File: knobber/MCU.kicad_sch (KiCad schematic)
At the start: 16 parts, among them J801 SWD, J802 Micro_SD_Card, U801 BMD-340-A-R, U802 ESD224DQA

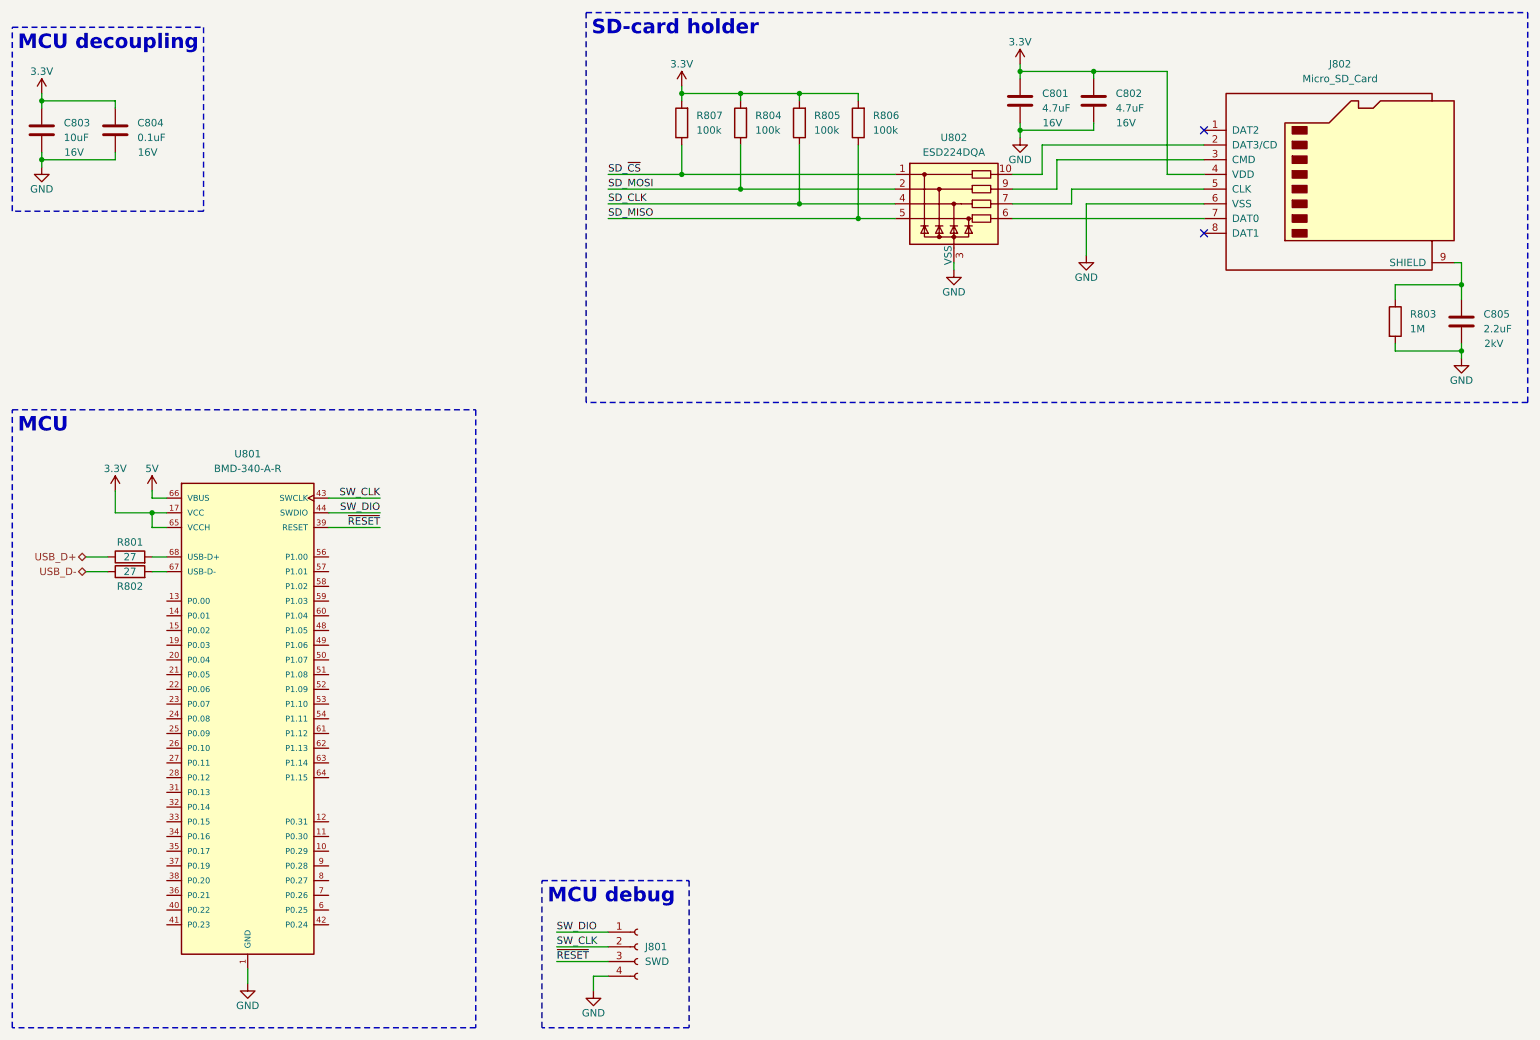
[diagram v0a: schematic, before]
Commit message: Updated schematic and PCB
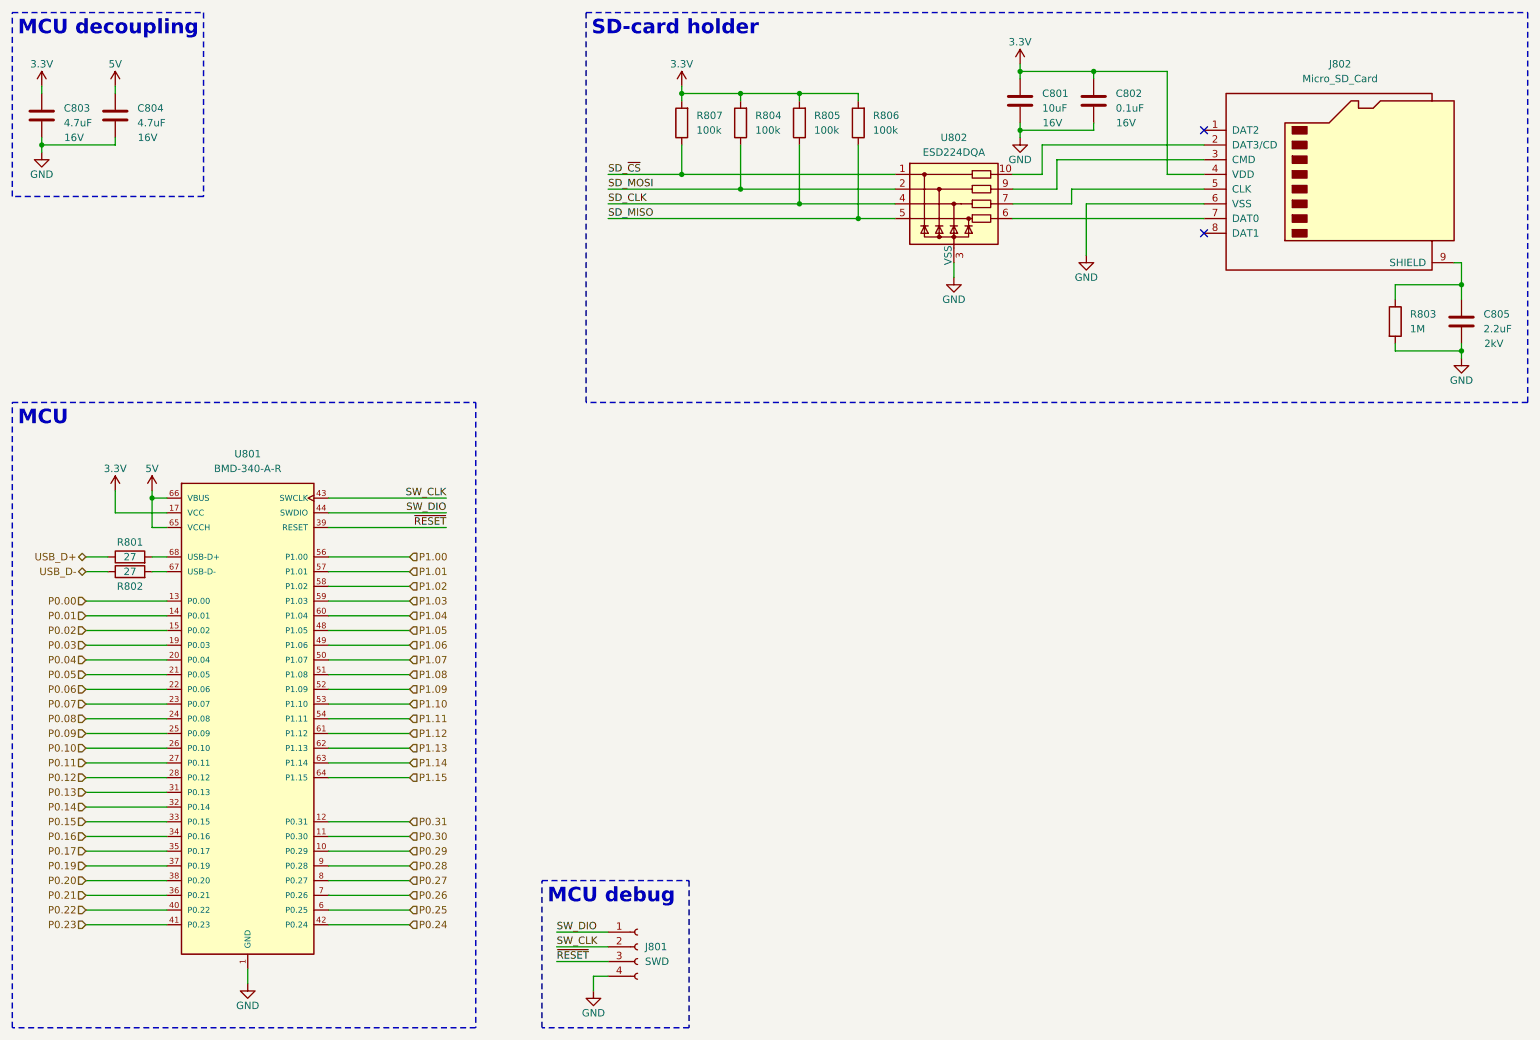
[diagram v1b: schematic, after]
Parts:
- C801: value 4.7uF -> 10uF
- C802: value 4.7uF -> 0.1uF
- C803: value 10uF -> 4.7uF
- C804: value 0.1uF -> 4.7uF
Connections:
- net 3.3V: no longer C804.1, U801.65 (VCCH)
- net 5V: now also C804.1, U801.65 (VCCH)
- net P0.29: now reaches U801.10 (P0.29)
- net P0.30: now reaches U801.11 (P0.30)
- net P0.31: now reaches U801.12 (P0.31)
- net P0.00: now reaches U801.13 (P0.00)
- net P0.01: now reaches U801.14 (P0.01)
- net P0.02: now reaches U801.15 (P0.02)
- net P0.03: now reaches U801.19 (P0.03)
- net P0.04: now reaches U801.20 (P0.04)
- net P0.05: now reaches U801.21 (P0.05)
- net P0.06: now reaches U801.22 (P0.06)
- net P0.07: now reaches U801.23 (P0.07)
- net P0.08: now reaches U801.24 (P0.08)
- net P0.09: now reaches U801.25 (P0.09)
- net P0.10: now reaches U801.26 (P0.10)
- net P0.11: now reaches U801.27 (P0.11)
- net P0.12: now reaches U801.28 (P0.12)
- net P0.13: now reaches U801.31 (P0.13)
- net P0.14: now reaches U801.32 (P0.14)
- net P0.15: now reaches U801.33 (P0.15)
- net P0.16: now reaches U801.34 (P0.16)
- net P0.17: now reaches U801.35 (P0.17)
- net P0.21: now reaches U801.36 (P0.21)
- net P0.19: now reaches U801.37 (P0.19)
- net P0.20: now reaches U801.38 (P0.20)
- net P0.22: now reaches U801.40 (P0.22)
- net P0.23: now reaches U801.41 (P0.23)
- net P0.24: now reaches U801.42 (P0.24)
- net P1.05: now reaches U801.48 (P1.05)
- net P1.06: now reaches U801.49 (P1.06)
- net P1.07: now reaches U801.50 (P1.07)
- net P1.08: now reaches U801.51 (P1.08)
- net P1.09: now reaches U801.52 (P1.09)
- net P1.10: now reaches U801.53 (P1.10)
- net P1.11: now reaches U801.54 (P1.11)
- net P1.00: now reaches U801.56 (P1.00)
- net P1.01: now reaches U801.57 (P1.01)
- net P1.02: now reaches U801.58 (P1.02)
- net P1.03: now reaches U801.59 (P1.03)
- net P0.25: now reaches U801.6 (P0.25)
- net P1.04: now reaches U801.60 (P1.04)
- net P1.12: now reaches U801.61 (P1.12)
- net P1.13: now reaches U801.62 (P1.13)
- net P1.14: now reaches U801.63 (P1.14)
- net P1.15: now reaches U801.64 (P1.15)
- net P0.26: now reaches U801.7 (P0.26)
- net P0.27: now reaches U801.8 (P0.27)
- net P0.28: now reaches U801.9 (P0.28)
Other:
- moved on the sheet: C803, C804
